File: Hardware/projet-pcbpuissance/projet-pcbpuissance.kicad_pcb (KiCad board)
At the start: 2 copper layers, 52.4 x 45.8 mm, 35 parts, among them J2 Conn_01x02, J3 Conn_01x02, J4 Conn_01x02, U1 MAX5033DUSA+, U2 MAX5033DUSA+

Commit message: Modif PCB
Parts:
- D2, D6: footprint Diode_SMD:D_SMA_Handsoldering -> Diode_SMD:D_2114_3652Metric_Pad1.85x3.75mm_HandSolder
- moved D6 0.51 mm to (110.7, 78.9)

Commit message: Modif PCB
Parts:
- moved H1 0.34 mm to (142.7, 72.7)
- moved H2 0.09 mm to (142.7, 108.5)
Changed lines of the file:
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@@
   )
   (footprint "MountingHole:MountingHole_3.2mm_M3_DIN965_Pad" (layer "F.Cu")
-    (at 142.8125 108.45)
+    (at 142.7225 108.45)
     (descr "Mounting Hole 3.2mm, M3, DIN965")
     (tags "mounting hole 3.2mm m3 din965")
@@
   )
   (footprint "MountingHole:MountingHole_3.2mm_M3_DIN965_Pad" (layer "F.Cu")
-    (at 100.4805 108.48)
+    (at 100.4805 108.45)
     (descr "Mounting Hole 3.2mm, M3, DIN965")
     (tags "mounting hole 3.2mm m3 din965")
@@
   )
   (footprint "MountingHole:MountingHole_3.2mm_M3_DIN965_Pad" (layer "F.Cu")
-    (at 142.8125 73)
+    (at 142.7225 72.676)
     (descr "Mounting Hole 3.2mm, M3, DIN965")
     (tags "mounting hole 3.2mm m3 din965")

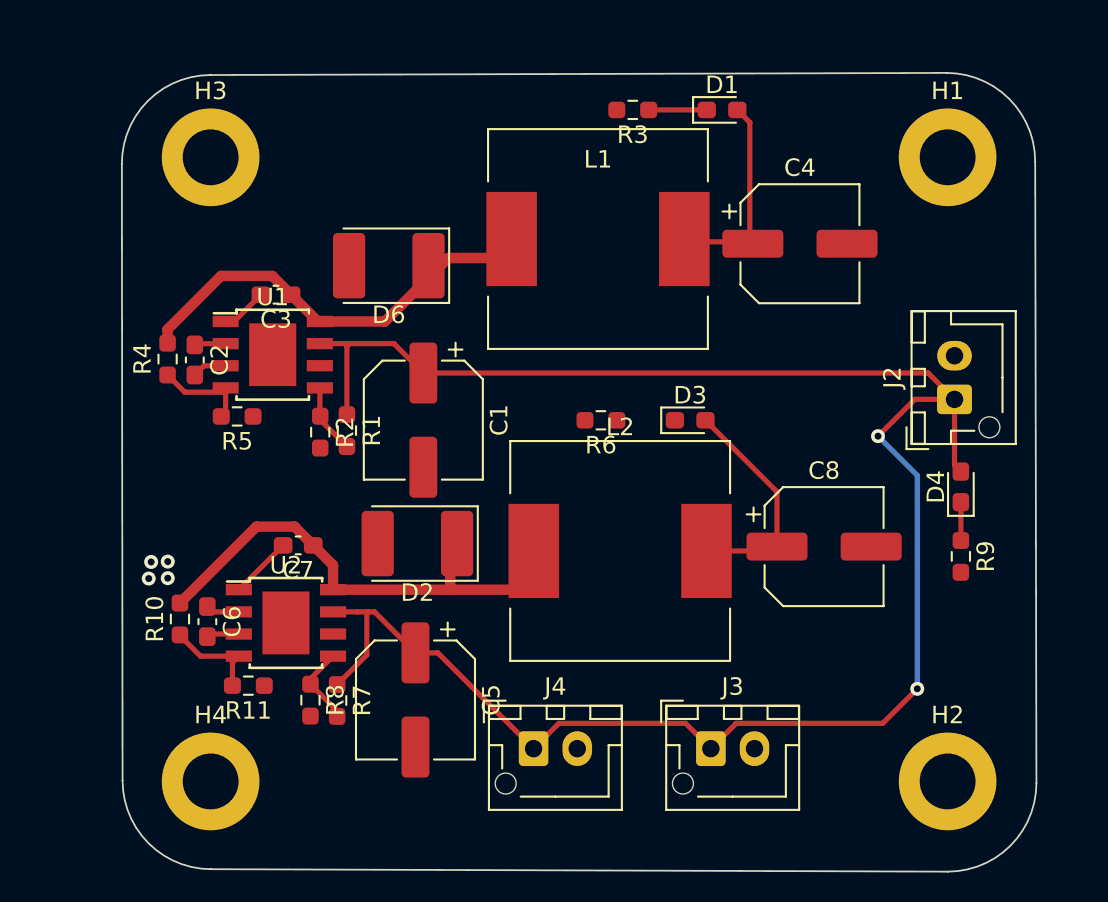
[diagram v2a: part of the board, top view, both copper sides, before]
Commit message: update with bigger vias and fix unrouted tracks
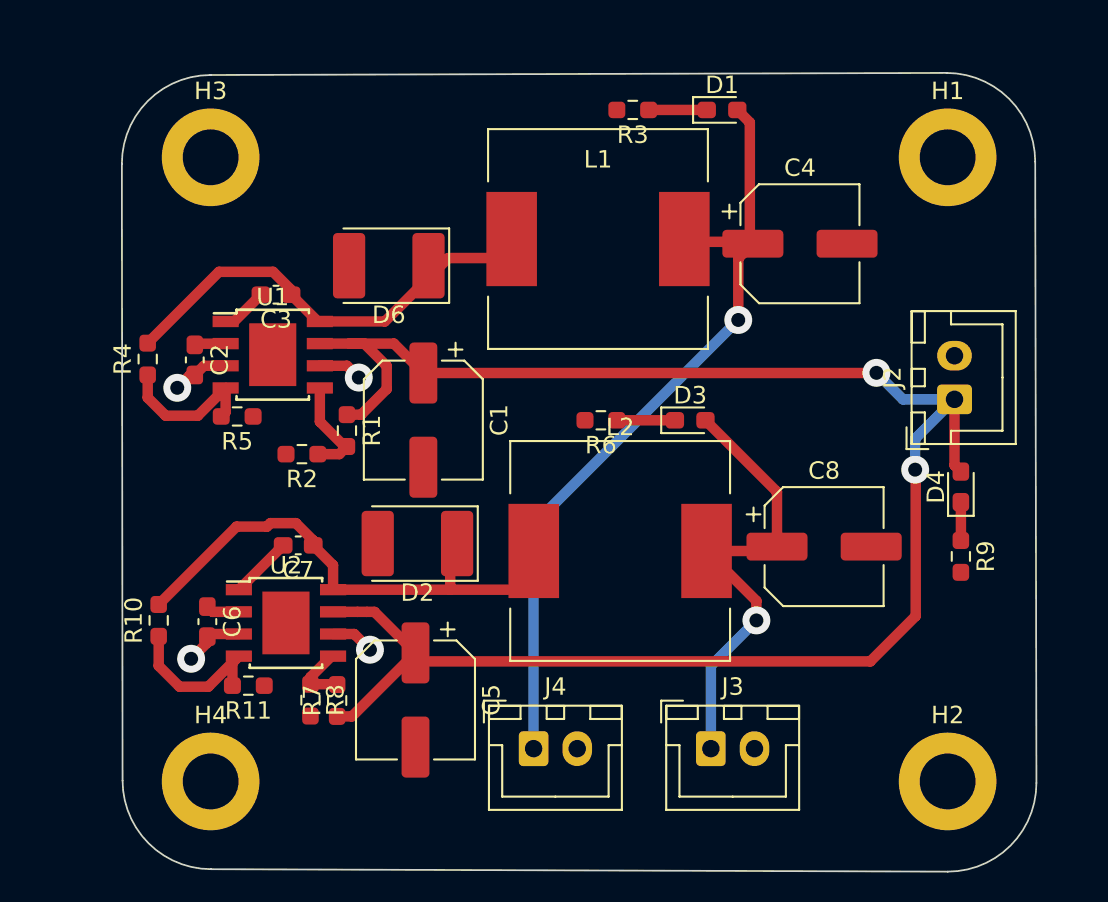
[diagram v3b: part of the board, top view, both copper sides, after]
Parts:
- J2, J3, J4: footprint Connector_JST:JST_XH_B2B-XH-AM_1x02_P2.50mm_Vertical -> Connector_JST:JST_XH_B2B-XH-A_1x02_P2.50mm_Vertical
- moved R2 1.64 mm to (105.7, 89.7), turned to 180 degrees
- moved R10 1.22 mm to (97.5, 99.2)
- moved R4 1.14 mm to (96.9, 84.2)
- turned R7 to 90 degrees
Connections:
- J3 pad 1: Batterie 11.1 V -> 7.4V
- J4 pad 1: Batterie 11.1 V -> +3.3V
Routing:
- net +3.3V: track 11.6 -> 45.8 mm, vias 0 -> 1
- net 7.4V: track 13.1 -> 26.7 mm, vias 0 -> 1
- net GND: track 3.85 -> 11.8 mm
- net Batterie 11.1 V: track 111.0 -> 103.9 mm
- net Net-(U2-FB): track 5.74 -> 9.35 mm
- net Net-(D3-K): track 0.00 -> 3.33 mm
- net Net-(U1-FB): track 5.58 -> 8.60 mm
- net Net-(U1-ON/~{OFF}): track 4.00 -> 5.93 mm
- net Net-(D2-K): track 27.4 -> 29.0 mm
- net Net-(D6-K): track 24.8 -> 25.9 mm
- net Net-(U2-ON/~{OFF}): track 4.62 -> 3.74 mm
